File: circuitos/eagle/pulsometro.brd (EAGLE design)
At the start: 83.5 x 69.2 mm, 33 parts, among them IC1 LM358N, IC2 LM358N, IC3 PIC18F2550_28DIP, T1 BC547, X1 20MHz

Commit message: Reduce amplifier resistor
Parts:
- R5: value 8.2k -> 4.6k
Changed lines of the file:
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@@
 <setting verticaltext="up"/>
 </settings>
-<grid distance="0.025" unitdist="inch" unit="inch" style="lines" multiple="2" display="yes" altdistance="0.005" altunitdist="inch" altunit="inch"/>
+<grid distance="0.05" unitdist="inch" unit="inch" style="lines" multiple="2" display="yes" altdistance="0.005" altunitdist="inch" altunit="inch"/>
 <layers>
 <layer number="1" name="Top" color="4" fill="1" visible="yes" active="yes"/>
@@
 <element name="R3" library="rcl" package="0204/7" value="820k" x="26.035" y="53.34"/>
 <element name="R4" library="rcl" package="0204/7" value="820k" x="22.86" y="72.39" rot="R90"/>
-<element name="R5" library="rcl" package="0204/7" value="8.2k" x="19.05" y="72.39" rot="R270"/>
+<element name="R5" library="rcl" package="0204/7" value="4.6k" x="19.05" y="72.39" rot="R270"/>
 <element name="R6" library="rcl" package="0204/7" value="931k" x="41.91" y="48.26" rot="R180"/>
 <element name="R7" library="rcl" package="0204/7" value="931k" x="52.705" y="66.675" rot="R270"/>

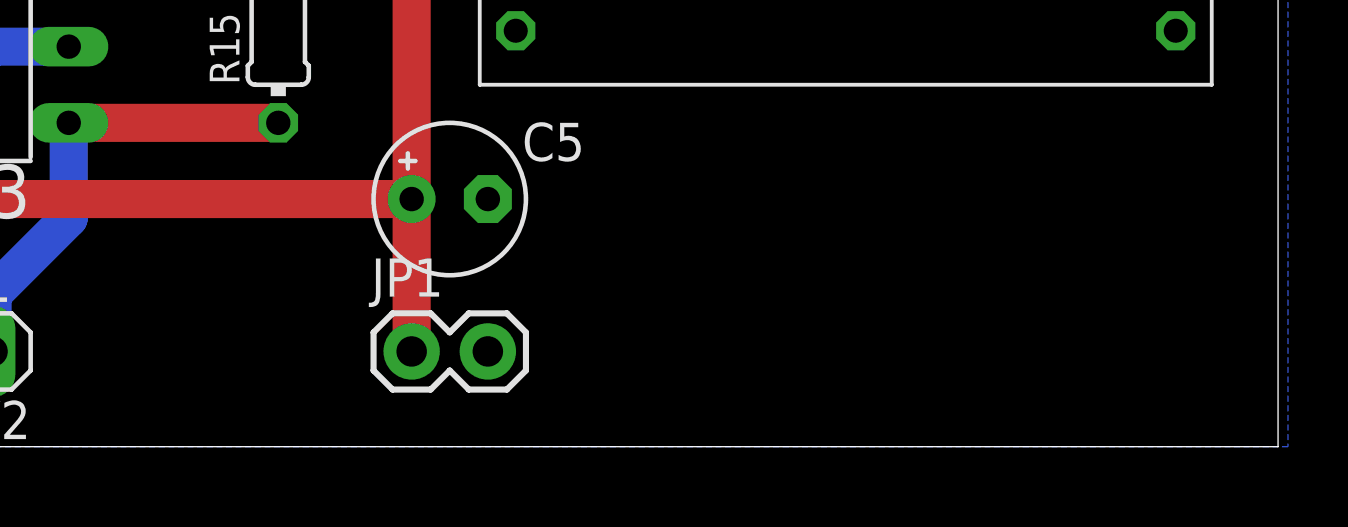
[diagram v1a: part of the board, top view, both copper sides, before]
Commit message: Add regulator to schematic and board
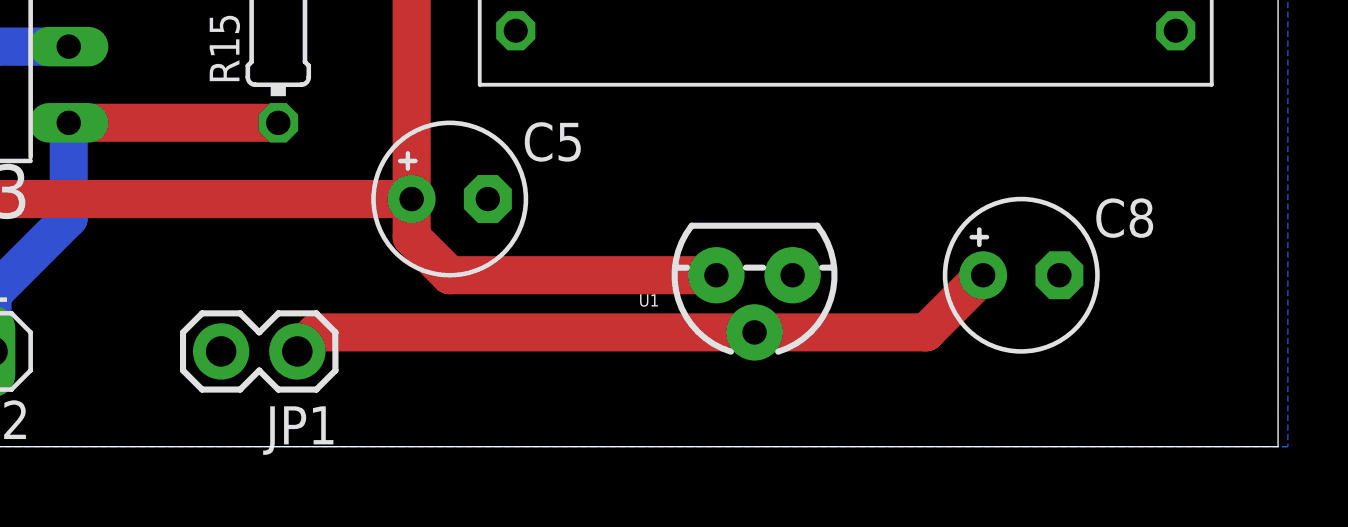
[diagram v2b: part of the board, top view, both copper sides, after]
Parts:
- added C8: 1u, rcl:E2,5-5
- added U1: (no value), SparkFun-PowerIC:TO-92
- moved JP1 3.81 mm to (66.0, 16.5), turned to 180 degrees
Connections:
- new net VBATT: C8.+, JP1.1, U1.2
- net +3V3: now also U1.3; no longer JP1.1
- net GND: now also C8.-, U1.1
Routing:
- net VBATT: track 0.00 -> 23.9 mm
- net +3V3: track 211.5 -> 218.4 mm
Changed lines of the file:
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@@
 <layer number="113" name="IDFDebug" color="4" fill="1" visible="no" active="yes"/>
 <layer number="116" name="Patch_BOT" color="9" fill="4" visible="no" active="yes"/>
+<layer number="118" name="Rect_Pads" color="7" fill="1" visible="yes" active="yes"/>
 <layer number="121" name="_tsilk" color="7" fill="1" visible="no" active="yes"/>
 <layer number="122" name="_bsilk" color="7" fill="1" visible="no" active="yes"/>
@@
 <element name="X1" library="IQD-Frequency-Products" package="HC49" value="20MHz" x="64.77" y="45.72" rot="R270"/>
 <element name="U$2" library="pulsometro" package="2X10-2MMSOCKET" value="RN42" x="96.52" y="25.4" rot="R90"/>
-<element name="JP1" library="SparkFun-Connectors" package="1X02" value="" x="69.85" y="16.51"/>
+<element name="JP1" library="SparkFun-Connectors" package="1X02" value="" x="66.04" y="16.51" rot="R180"/>
+<element name="U1" library="SparkFun-PowerIC" package="TO-92" value="" x="81.28" y="19.05" rot="R180"/>
+<element name="C8" library="rcl" package="E2,5-5" value="1u" x="90.17" y="19.05"/>
 </elements>
 <signals>
@@
 <contactref element="R15" pad="2"/>
 <contactref element="U$2" pad="PIN1"/>
-<contactref element="JP1" pad="1"/>
 <wire x1="29.845" y1="65.405" x2="33.02" y2="68.58" width="1.27" layer="16"/>
 <wire x1="29.845" y1="58.42" x2="29.845" y2="65.405" width="1.27" layer="16"/>
@@
 <wire x1="27.94" y1="58.42" x2="29.845" y2="58.42" width="1.27" layer="1"/>
 <wire x1="22.225" y1="47.625" x2="26.035" y2="47.625" width="1.27" layer="1"/>
-<wire x1="69.85" y1="21.59" x2="69.85" y2="16.51" width="1.27" layer="1"/>
 <wire x1="54.61" y1="21.59" x2="69.85" y2="21.59" width="1.27" layer="1"/>
+<contactref element="U1" pad="3"/>
+<wire x1="80.01" y1="19.05" x2="71.12" y2="19.05" width="1.27" layer="1"/>
+<wire x1="71.12" y1="19.05" x2="69.85" y2="20.32" width="1.27" layer="1"/>
+<wire x1="69.85" y1="20.32" x2="69.85" y2="21.59" width="1.27" layer="1"/>
 </signal>
 <signal name="N$3">
@@
 <contactref element="U$2" pad="PIN10"/>
 <contactref element="JP1" pad="2"/>
+<contactref element="U1" pad="1"/>
+<contactref element="C8" pad="-"/>
 </signal>
 <signal name="N$4">
@@
 </polygon>
 </signal>
+<signal name="VBATT">
+<contactref element="JP1" pad="1"/>
+<contactref element="U1" pad="2"/>
+<contactref element="C8" pad="+"/>
+<wire x1="81.28" y1="17.145" x2="66.675" y2="17.145" width="1.27" layer="1"/>
+<wire x1="66.675" y1="17.145" x2="66.04" y2="16.51" width="1.27" layer="1"/>
+<wire x1="81.28" y1="17.145" x2="86.995" y2="17.145" width="1.27" layer="1"/>
+<wire x1="86.995" y1="17.145" x2="88.9" y2="19.05" width="1.27" layer="1"/>
+</signal>
 </signals>

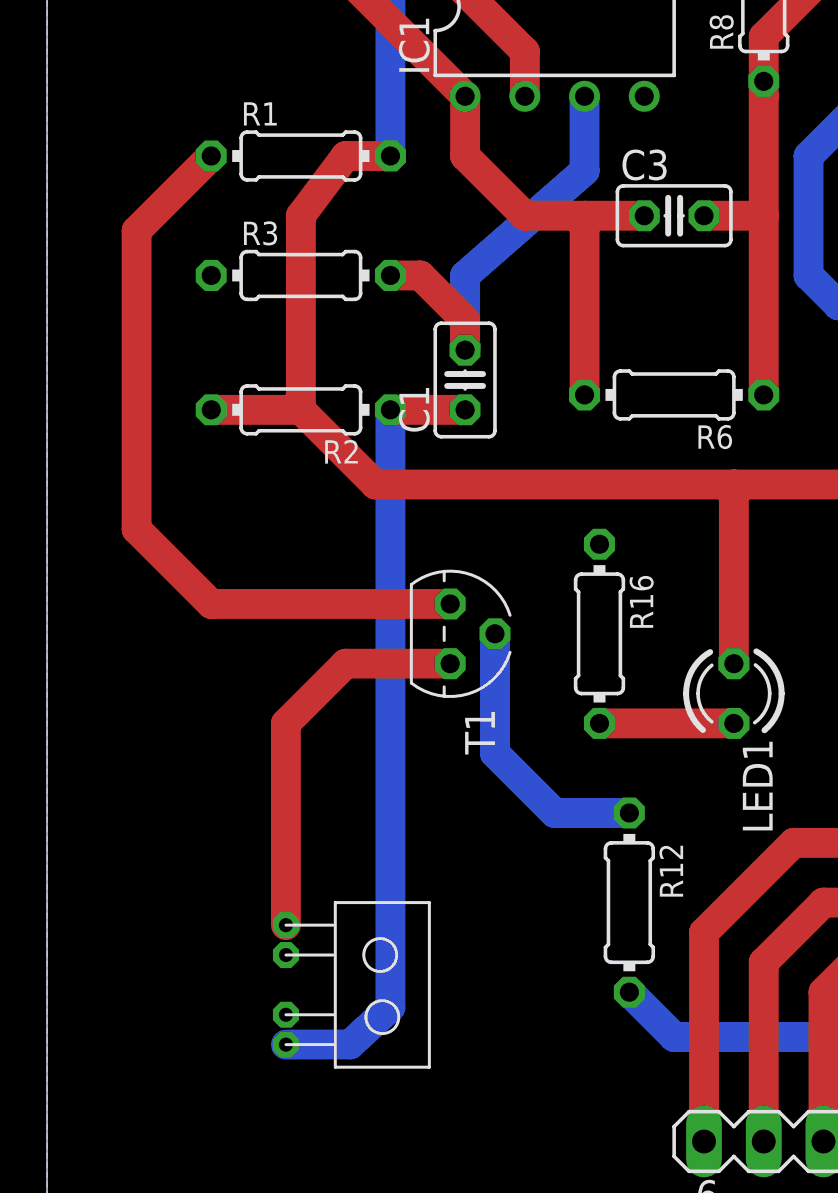
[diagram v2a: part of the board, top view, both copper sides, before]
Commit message: Update circuit
* Remove transistor switch of TCRT1010 diode and change resistor value
* Change LM358 op-amp to TLV2472
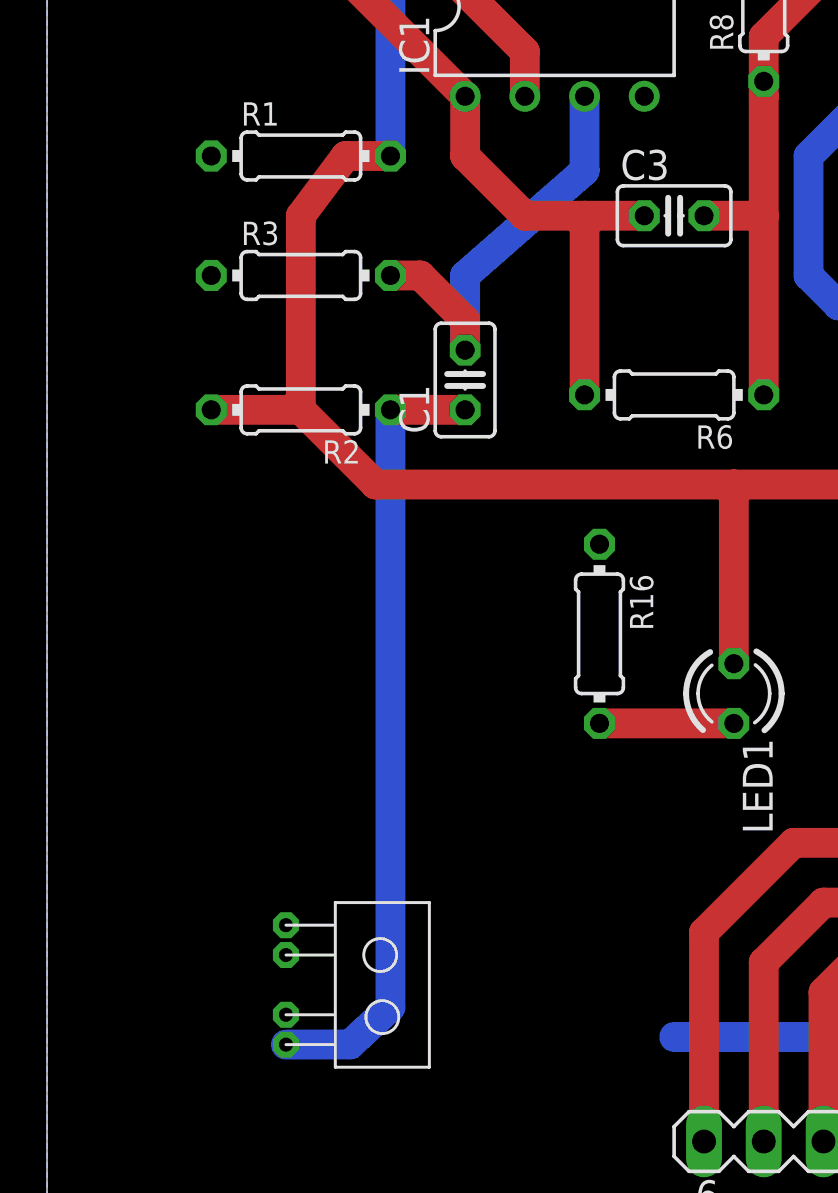
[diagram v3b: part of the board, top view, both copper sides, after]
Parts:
- removed R12: 10k, rcl:0204/7
- removed T1: BC547, transistor:TO92
- IC1, IC2: value LM358N -> TLV2472
- R1: value 160 -> 220
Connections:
- removed net N$2: T1.1, U$1.PIN_1
- removed net N$7: R12.1, T1.2
- net N$1: now also U$1.PIN_1; no longer T1.3
- net RA0: no longer R12.2
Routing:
- net N$1: track 31.8 -> 0.00 mm
- net N$2: track 16.6 -> 0.00 mm
- net N$7: track 11.8 -> 0.00 mm
- net RA0: track 23.4 -> 20.7 mm
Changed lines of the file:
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@@
 <element name="C6" library="rcl" package="C025-025X050" value="15n" x="66.675" y="36.83" rot="R90"/>
 <element name="C7" library="rcl" package="C025-025X050" value="15n" x="62.23" y="36.83" rot="R90"/>
-<element name="IC1" library="linear" package="DIL08" value="LM358N" x="36.83" y="64.77"/>
-<element name="IC2" library="linear" package="DIL08" value="LM358N" x="64.77" y="68.58" rot="R180"/>
+<element name="IC1" library="linear" package="DIL08" value="TLV2472" x="36.83" y="64.77"/>
+<element name="IC2" library="linear" package="DIL08" value="TLV2472" x="64.77" y="68.58" rot="R180"/>
 <element name="IC3" library="microchip" package="DIL28-3" value="PIC18F2550_28DIP" x="54.61" y="40.64" rot="R90">
 <attribute name="OC_NEWARK" value="80K6054" x="54.61" y="40.64" size="1.778" layer="27" rot="R90" display="off"/>
@@
 </element>
 <element name="LED1" library="led" package="LED3MM" value="" x="44.45" y="35.56" rot="R270"/>
-<element name="R1" library="rcl" package="0204/7" value="160" x="26.035" y="58.42"/>
+<element name="R1" library="rcl" package="0204/7" value="220" x="26.035" y="58.42"/>
 <element name="R10" library="rcl" package="0204/7" value="47k" x="48.895" y="74.93" rot="R90"/>
 <element name="R11" library="rcl" package="0204/7" value="42k" x="66.04" y="76.2"/>
-<element name="R12" library="rcl" package="0204/7" value="10k" x="40.005" y="26.67" rot="R270"/>
 <element name="R13" library="rcl" package="PT-10" value="100k" x="78.74" y="71.755" rot="R180"/>
 <element name="R14" library="rcl" package="PT-10" value="10k" x="91.44" y="71.755" rot="R180"/>
@@
 <attribute name="OC_FARNELL" value="unknown" x="49.53" y="16.51" size="1.778" layer="27" rot="R180" display="off"/>
 </element>
-<element name="T1" library="transistor" package="TO92" value="BC547" x="32.385" y="38.1" rot="R270"/>
 <element name="U$1" library="pulsometro" package="TCRT1010" value="TCRT1010" x="25.4" y="26.67" rot="R270"/>
 <element name="X1" library="IQD-Frequency-Products" package="HC49" value="20MHz" x="64.77" y="45.72" rot="R270"/>
@@
 </elements>
 <signals>
-<signal name="N$1">
-<contactref element="R1" pad="1"/>
-<contactref element="T1" pad="3"/>
-<wire x1="22.225" y1="39.37" x2="32.385" y2="39.37" width="1.27" layer="1"/>
-<wire x1="19.05" y1="42.545" x2="22.225" y2="39.37" width="1.27" layer="1"/>
-<wire x1="19.05" y1="55.245" x2="19.05" y2="42.545" width="1.27" layer="1"/>
-<wire x1="22.225" y1="58.42" x2="19.05" y2="55.245" width="1.27" layer="1"/>
-</signal>
-<signal name="N$2">
-<contactref element="U$1" pad="PIN_1"/>
-<contactref element="T1" pad="1"/>
-<wire x1="25.4" y1="25.71" x2="25.4" y2="34.29" width="1.27" layer="1"/>
-<wire x1="25.4" y1="34.29" x2="27.94" y2="36.83" width="1.27" layer="1"/>
-<wire x1="27.94" y1="36.83" x2="32.385" y2="36.83" width="1.27" layer="1"/>
-</signal>
 <signal name="+3V3">
 <contactref element="R1" pad="2"/>
@@
 <wire x1="30.48" y1="71.12" x2="27.94" y2="71.12" width="1.27" layer="16"/>
 </signal>
-<signal name="N$7">
-<contactref element="T1" pad="2"/>
-<contactref element="R12" pad="1"/>
-<wire x1="40.005" y1="30.48" x2="36.83" y2="30.48" width="1.27" layer="16"/>
-<wire x1="36.83" y1="30.48" x2="34.29" y2="33.02" width="1.27" layer="16"/>
-<wire x1="34.29" y1="33.02" x2="34.29" y2="38.1" width="1.27" layer="16"/>
-</signal>
 <signal name="RA0">
-<contactref element="R12" pad="2"/>
 <contactref element="IC3" pad="2"/>
-<wire x1="40.005" y1="22.86" x2="41.91" y2="20.955" width="1.27" layer="16"/>
 <wire x1="41.91" y1="20.955" x2="53.34" y2="20.955" width="1.27" layer="16"/>
 <wire x1="53.34" y1="20.955" x2="54.61" y2="22.225" width="1.27" layer="16"/>
@@
 <wire x1="86.995" y1="17.145" x2="88.9" y2="19.05" width="1.27" layer="1"/>
 </signal>
+<signal name="N$1">
+<contactref element="U$1" pad="PIN_1"/>
+<contactref element="R1" pad="1"/>
+<wire x1="25.4" y1="25.71" x2="22.225" y2="58.42" width="0" layer="19" extent="1-1"/>
+</signal>
 </signals>

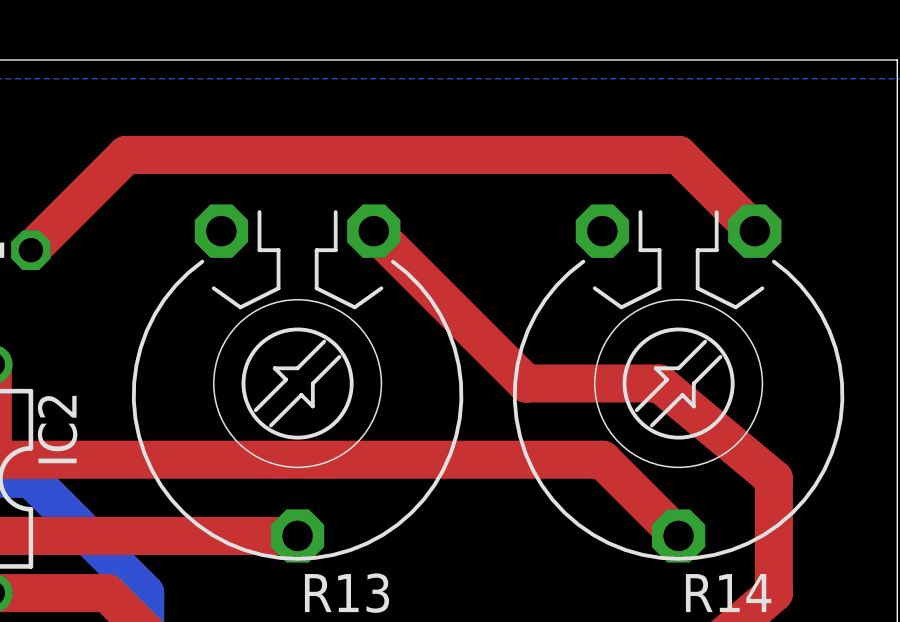
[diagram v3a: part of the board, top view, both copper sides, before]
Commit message: Fix voltage source value
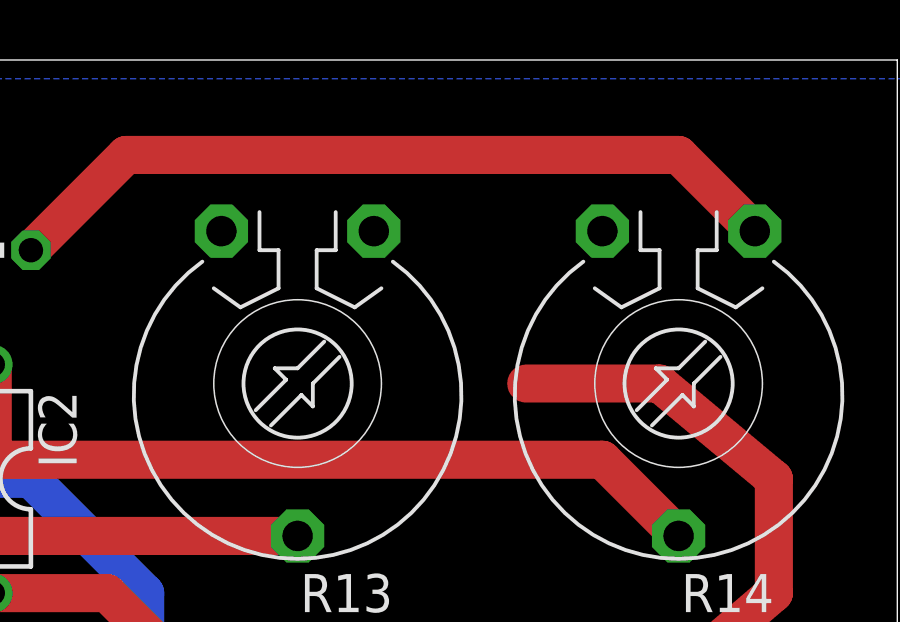
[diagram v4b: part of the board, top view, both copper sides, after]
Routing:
- net +3V3: track 218.4 -> 211.2 mm
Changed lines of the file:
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@@
 <signal name="+3V3">
 <contactref element="R1" pad="2"/>
-<contactref element="R13" pad="1"/>
 <contactref element="IC3" pad="20"/>
 <contactref element="SV2" pad="2"/>
@@
 <wire x1="94.615" y1="68.58" x2="90.805" y2="71.755" width="1.27" layer="1"/>
 <wire x1="90.805" y1="71.755" x2="86.36" y2="71.755" width="1.27" layer="1"/>
-<wire x1="86.36" y1="71.755" x2="81.28" y2="76.835" width="1.27" layer="1"/>
 <wire x1="50.8" y1="44.45" x2="53.34" y2="44.45" width="1.27" layer="1"/>
 <wire x1="53.34" y1="44.45" x2="54.61" y2="43.18" width="1.27" layer="1"/>
@@
 <wire x1="71.12" y1="19.05" x2="69.85" y2="20.32" width="1.27" layer="1"/>
 <wire x1="69.85" y1="20.32" x2="69.85" y2="21.59" width="1.27" layer="1"/>
+<contactref element="R13" pad="1"/>
+<wire x1="86.36" y1="71.755" x2="81.28" y2="76.835" width="0" layer="19" extent="1-1"/>
 </signal>
 <signal name="N$3">
